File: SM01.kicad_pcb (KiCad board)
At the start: 2 copper layers, 150 parts, among them J1 TRIG IN, J2 TRIG IN, J3 TRIG IN, J4 DC JACK, J5 TRIG IN, J6 VCA IN, J7 MIXOUT, Q1 2N3904, SW1 HOLD, SW10 SPDT_small, SW11 SPDT_small, SW12 MOM, SW13 SPDT_small, SW14 MOM, SW15 MOM, SW16 MOM, SW17 MOM, SW18 MOM, SW19 MOM, SW2 HOLD, SW20 MOM, SW21 MASTERSW, SW3 HOLD, SW4 ON, SW5 MOM, SW6 MOM, SW7 MOM, SW8 HOLD, SW9 SPDT_small, U1 072, U10 072, U11 072, U2 072, U3 072, U4 7414, U5 7414, U6 7414, U8 072, U9 072

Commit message: organized channels
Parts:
- moved C27 260.7 mm to (100.3, 182.9)
- moved R39 249.5 mm to (113.0, 182.9)
- moved C23 242.9 mm to (100.3, 179.1)
- moved C20 235.9 mm to (100.3, 175.3)
- moved C15 209.2 mm to (108.0, 168.9)
- moved U6 206.0 mm to (101.6, 143.5)
- moved SW4 203.6 mm to (185.4, 143.5)
- moved LED3 201.2 mm to (114.3, 144.8)
- moved MASTERV1 200.7 mm to (222.2, 33.0)
- moved R17 196.5 mm to (106.7, 120.7)
- moved OSC3 196.2 mm to (105.4, 132.1)
- moved C12 194.1 mm to (100.3, 168.9)
- moved C30 193.0 mm to (115.6, 168.9)
- moved R23 191.2 mm to (120.7, 113.0)
- moved R7 190.4 mm to (200.7, 130.8)
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
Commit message: continued laying out pcb - having issue with zfoot.pretty
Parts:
- removed LED1, LED2, LED3: LED-C1-A2, 4ms-footprints:LED-C1-A2-3MM-VERT
- removed SW12, SW5, SW6, SW7: MOM, 4ms-footprints:SPDT-SUB
- added LEDSW1: DPDT-ILLUM, 4ms-footprints:BUTTON-LED-PB61303, F.Cu at (10.0, -10.0)
- added LEDSW2: DPDT-ILLUM, 4ms-footprints:BUTTON-LED-PB61303, F.Cu at (50.0, -10.0)
- added LEDSW3: DPDT-ILLUM, 4ms-footprints:BUTTON-LED-PB61303, F.Cu at (90.0, -10.0)
- added LEDSW4: DPDT-ILLUM, 4ms-footprints:BUTTON-LED-PB61303, F.Cu at (130.0, -10.0)
- added R50: 470, 4ms-footprints:Resistor_TH_300, B.Cu at (115.6, 63.7)
- C1, C10, C11, C12, C13, C14, C15, C16, C17, C18, C19, C2, C20, C21, C22, C23, C24, C25, C26, C27, C28, C29, C3, C30, C31, C32, C4, C5, C6, C7, C8, C9, D1, D2, D3, D4, D5, D6, J4, Q1, R1, R10, R11, R12, R13, R14, R15, R16, R17, R18, R19, R20, R21, R22, R23, R24, R25, R26, R27, R28, R29, R3, R30, R31, R32, R33, R34, R35, R36, R37, R38, R39, R4, R40, R41, R42, R43, R44, R45, R46, R47, R48, R49, R5, R6, R7, R8, R9, SW4, U1, U10, U11, U2, U3, U4, U5, U6, U8, U9, VREG1: moved to B.Cu
- SW10: value SPDT_small -> DECAYSW2
- SW11: value SPDT_small -> DECAYSW3
- SW13: value SPDT_small -> DECAYSW4
- SW14: value MOM -> OSCSW1
- SW15: value MOM -> OSCSW2
- SW16: value MOM -> OSCSW3
- SW17: value MOM -> MUTE4
- SW18: value MOM -> MUTE1
- SW19: value MOM -> MUTE2
- SW20: value MOM -> MUTE3
- SW9: value SPDT_small -> DECAYSW1
- moved VOL1 230.1 mm to (170.0, -85.0)
- moved C18 218.1 mm to (18.4, -28.9)
- moved R28 215.4 mm to (25.4, -40.6)
- moved C28 214.2 mm to (10.0, -46.8), turned to 90 degrees
- moved C10 213.5 mm to (30.0, -47.0), turned to 90 degrees
- moved C13 213.3 mm to (20.0, -46.9), turned to 90 degrees
- moved R21 207.9 mm to (30.0, -29.6), turned to 180 degrees
- moved J6 202.9 mm to (142.5, -95.0)
- moved SW20 199.7 mm to (190.0, -47.5)
- moved C25 193.9 mm to (21.6, -35.6)
- moved R15 193.2 mm to (12.5, -73.1), turned to 270 degrees
- moved C21 190.8 mm to (21.1, -7.39), turned to 90 degrees
- moved R31 189.5 mm to (18.5, -10.9), turned to 90 degrees
- moved R24 185.0 mm to (23.6, -10.9), turned to 90 degrees
- moved SW17 183.8 mm to (190.0, -28.8)
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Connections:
- R1 pad 1: Net-(R1-Pad1) -> Net-(J1-Pad1)
- R18 pad 1: Net-(R18-Pad1) -> Net-(J5-Pad1)
- R2 pad 1: Net-(R2-Pad1) -> Net-(J2-Pad1)
- R3 pad 1: Net-(R3-Pad1) -> Net-(J3-Pad1)
- SW1 pad 3: Net-(R1-Pad1) -> Net-(J1-Pad1)
- SW2 pad 3: Net-(R2-Pad1) -> Net-(J2-Pad1)
- SW3 pad 3: Net-(R3-Pad1) -> Net-(J3-Pad1)
- SW8 pad 3: Net-(R18-Pad1) -> Net-(J5-Pad1)
- U11 pad 5: Net-(U11-Pad5) -> Net-(ATTACK4-Pad2)
- U11 pad 6: Net-(U11-Pad6) -> LED_AR
- U11 pad 7: Net-(U11-Pad7) -> LED_AR
- U4 pad 14: Net-(U1-Pad6) -> Net-(C10-Pad1)
- U5 pad 14: Net-(U2-Pad6) -> Net-(C11-Pad1)
- U6 pad 14: Net-(U3-Pad6) -> Net-(C12-Pad1)
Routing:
- net GND: track 0.00 -> 65.7 mm, vias 0 -> 1
- net Net-(R1-Pad2): track 0.00 -> 16.5 mm, vias 0 -> 2
- net Net-(J1-Pad1): track 0.00 -> 9.36 mm
- net Net-(ATTACK1-Pad2): track 0.00 -> 7.31 mm
- net Net-(D2-Pad2): track 0.00 -> 5.84 mm
- net Net-(ATTACK1-Pad1): track 0.00 -> 4.01 mm
- net Net-(U1-Pad6): track 0.00 -> 2.54 mm
- net Net-(DECAY1-Pad1): track 0.00 -> 2.29 mm
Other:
- board outline added: 200 x 100 mm
- net class Default: clearance 0.2 -> 0
- rule trace_clearance: 0.2 -> 0

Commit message: finished placing components - starting to connect traces
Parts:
- added J10: EXP3, zfoot:Jack_Instrument_exp, F.Cu at (102.6, -95.0)
- added J8: EXP1, zfoot:Jack_Instrument_exp, F.Cu at (22.6, -95.0)
- added J9: EXP2, zfoot:Jack_Instrument_exp, F.Cu at (62.7, -95.0)
- J4, SW4: moved to F.Cu
- R2: moved to B.Cu
- moved R38 266.3 mm to (181.0, -54.1)
- moved C32 211.5 mm to (158.8, -51.1)
- moved C11 210.2 mm to (70.0, -47.0), turned to 90 degrees
- moved C12 209.9 mm to (110.0, -47.0), turned to 90 degrees
- moved C14 208.5 mm to (60.0, -47.0), turned to 90 degrees
- moved C29 208.4 mm to (50.0, -47.0), turned to 90 degrees
- moved C15 208.4 mm to (100.0, -47.0), turned to 90 degrees
- moved C30 208.3 mm to (90.0, -47.0), turned to 90 degrees
- moved R39 205.6 mm to (191.0, -34.8), turned to 180 degrees
- moved U8 202.1 mm to (145.0, -69.0), turned to 90 degrees
- moved R3 201.6 mm to (100.0, -85.0), turned to 270 degrees
- moved U3 201.3 mm to (105.0, -69.0), turned to 90 degrees
- moved U2 201.3 mm to (65.0, -69.0), turned to 90 degrees
- moved R18 200.7 mm to (140.0, -85.0), turned to 270 degrees
- moved R48 193.9 mm to (151.4, -51.1), turned to 180 degrees
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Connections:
- VOL1 pad 1: Net-(R40-Pad1) -> Net-(R41-Pad1)
- VOL1 pad 2: Net-(R44-Pad2) -> Net-(R45-Pad2)
- VOL2 pad 1: Net-(R41-Pad1) -> Net-(R42-Pad1)
- VOL2 pad 2: Net-(R45-Pad2) -> Net-(R46-Pad2)
- VOL3 pad 1: Net-(R42-Pad1) -> Net-(R43-Pad1)
- VOL3 pad 2: Net-(R46-Pad2) -> Net-(R47-Pad2)
- VOL4 pad 1: Net-(R43-Pad1) -> Net-(R40-Pad1)
- VOL4 pad 2: Net-(R47-Pad2) -> Net-(R44-Pad2)
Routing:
- net GND: track 65.7 -> 0.85 mm, vias 1 -> 0
- net Net-(R1-Pad2): track 16.5 -> 0.00 mm, vias 2 -> 0
- net Net-(J1-Pad1): track 9.36 -> 0.01 mm
- net Net-(ATTACK1-Pad2): track 7.31 -> 2.65 mm
- net Net-(ATTACK1-Pad1): track 4.01 -> 0.40 mm
- net Net-(D2-Pad2): track 5.84 -> 3.15 mm
- net Net-(J8-Pad1): track 0.00 -> 2.54 mm
- net Net-(U1-Pad6): track 2.54 -> 0.00 mm
- net Net-(DECAY1-Pad1): track 2.29 -> 0.03 mm

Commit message: finished channel 1 but theres so much more bullshit left
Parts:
- moved J4 19.6 mm to (195.3, -95.0)
- moved SW4 5.00 mm to (180.0, -95.0)
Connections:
- J10 pad 2: Net-(J10-Pad1) -> Net-(J10-Pad2)
- J8 pad 2: Net-(J8-Pad1) -> Net-(J8-Pad2)
- J9 pad 2: Net-(J9-Pad1) -> Net-(J9-Pad2)
- R37 pad 1: Net-(J8-Pad1) -> Net-(J8-Pad2)
- R38 pad 1: Net-(J9-Pad1) -> Net-(J9-Pad2)
- R39 pad 1: Net-(J10-Pad1) -> Net-(J10-Pad2)
- U4 pad 6: Net-(J8-Pad1) -> Net-(J8-Pad2)
- U5 pad 6: Net-(J9-Pad1) -> Net-(J9-Pad2)
- U6 pad 6: Net-(J10-Pad1) -> Net-(J10-Pad2)
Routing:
- net GND: track 0.85 -> 913.8 mm, vias 0 -> 46
- net +5V: track 0.00 -> 687.0 mm, vias 0 -> 25
- net Net-(J8-Pad2): track 0.00 -> 295.2 mm, vias 0 -> 9
- net Net-(J1-Pad1): track 0.01 -> 131.5 mm, vias 0 -> 5
- net Net-(D1-Pad2): track 0.00 -> 108.2 mm, vias 0 -> 6
- net Net-(R48-Pad2): track 0.00 -> 95.8 mm, vias 0 -> 4
- net Net-(J8-Pad1): track 2.54 -> 75.3 mm, vias 0 -> 3
- net Net-(C25-Pad1): track 0.00 -> 67.5 mm, vias 0 -> 5
- net Net-(C13-Pad1): track 0.00 -> 55.5 mm, vias 0 -> 3
- net Net-(ATTACK1-Pad2): track 2.65 -> 54.9 mm, vias 0 -> 3
- net 2.5v: track 0.00 -> 50.0 mm, vias 0 -> 4
- net Net-(J5-Pad1): track 0.00 -> 42.7 mm, vias 0 -> 5
- net Net-(R1-Pad2): track 0.00 -> 42.7 mm, vias 0 -> 3
- net Net-(R41-Pad1): track 0.00 -> 38.9 mm, vias 0 -> 3
- net Net-(R45-Pad2): track 0.00 -> 37.7 mm, vias 0 -> 1
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
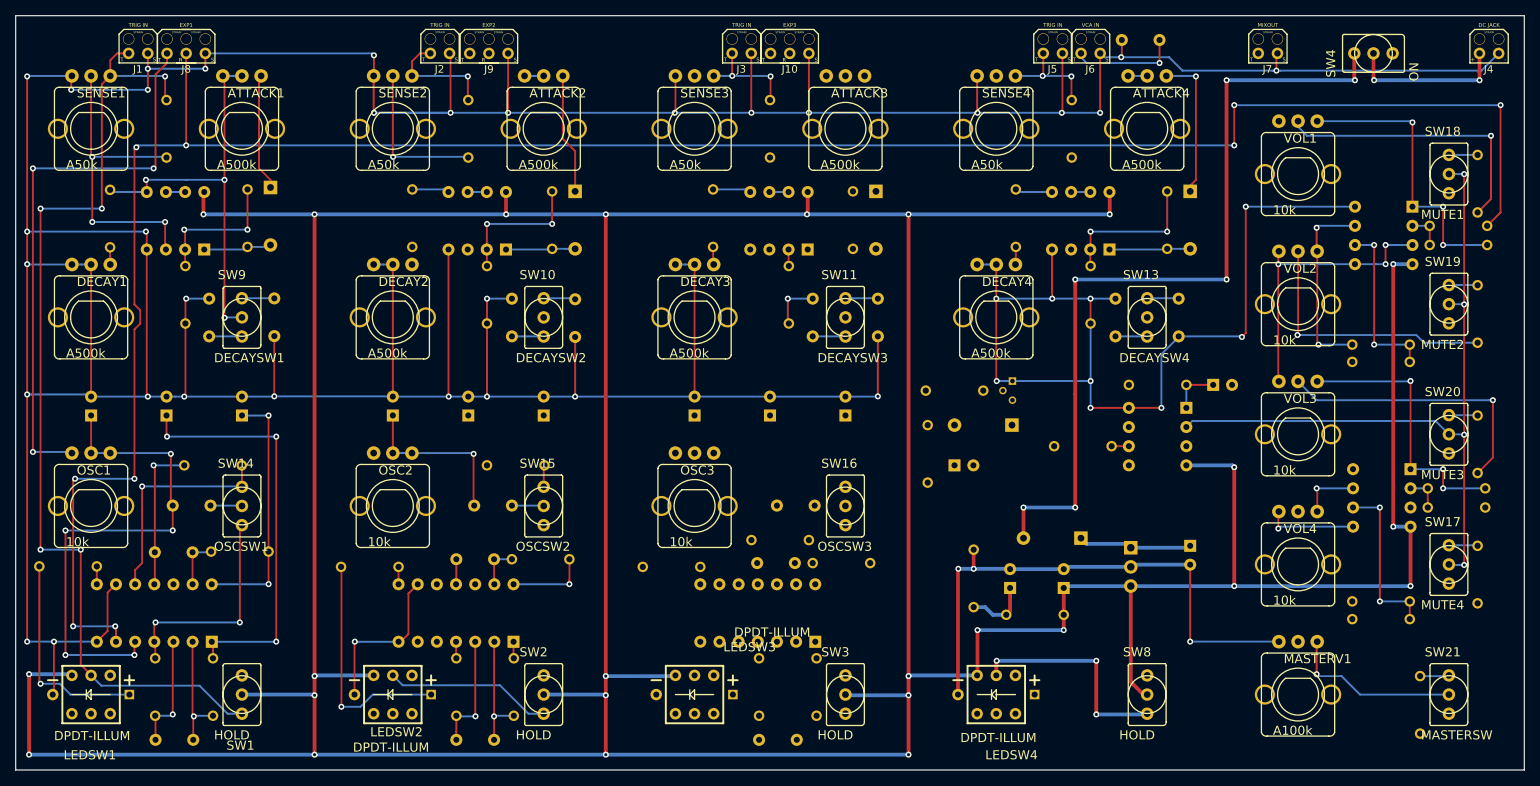
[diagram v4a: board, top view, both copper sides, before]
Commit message: finished laying traces and organizing ref
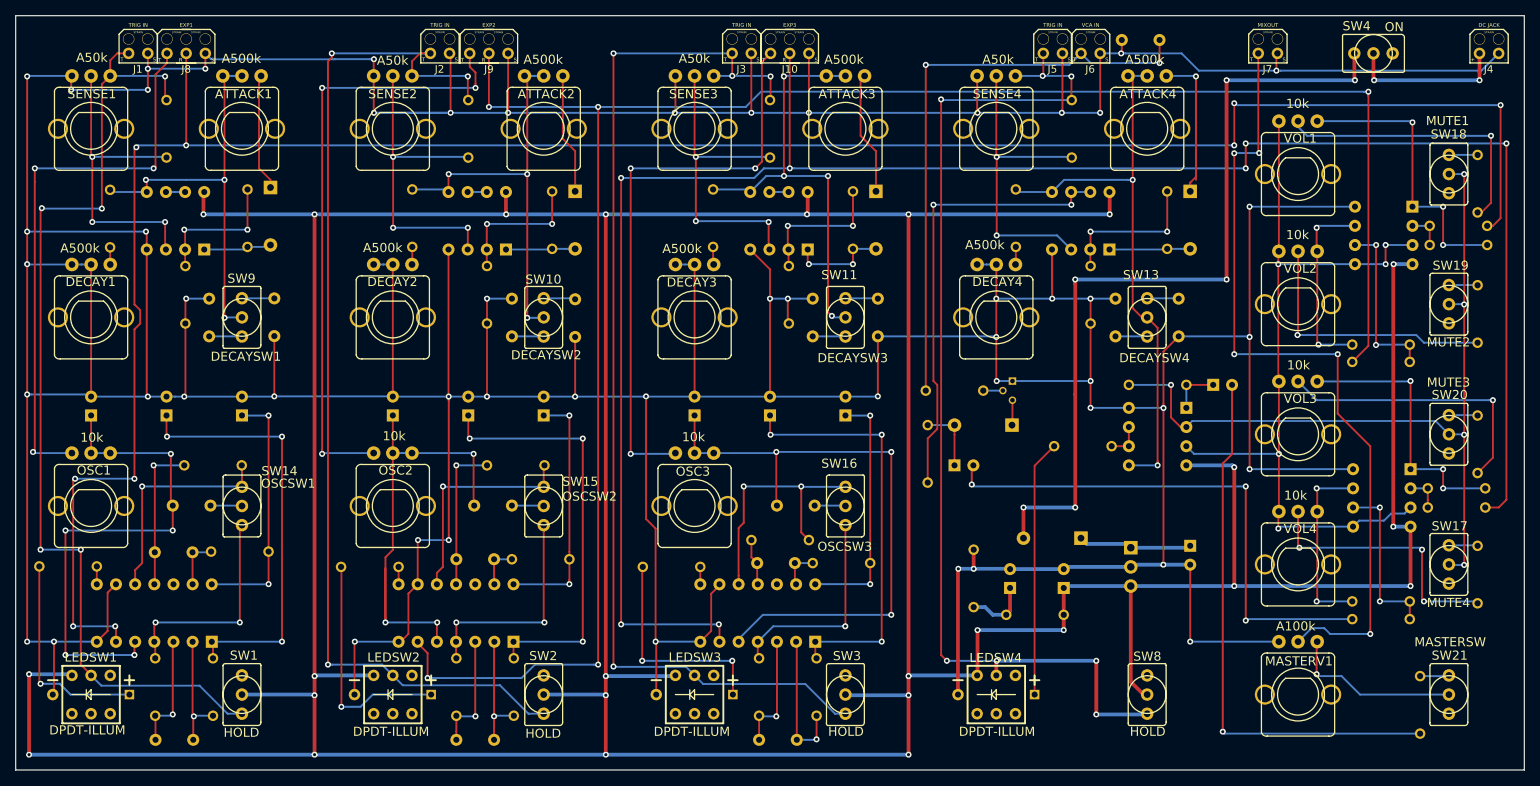
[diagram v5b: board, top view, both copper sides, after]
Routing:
- net Net-(J9-Pad2): track 0.00 -> 263.8 mm, vias 0 -> 5
- net Net-(J10-Pad2): track 0.00 -> 261.4 mm, vias 0 -> 7
- net GND: track 913.8 -> 1088.2 mm, vias 46 -> 54
- net Net-(J3-Pad1): track 13.7 -> 144.1 mm, vias 2 -> 4
- net Net-(J7-Pad1): track 0.00 -> 106.4 mm, vias 0 -> 5
- net Net-(J2-Pad1): track 37.5 -> 141.0 mm, vias 1 -> 3
- net Net-(J5-Pad1): track 42.7 -> 141.4 mm, vias 5 -> 7
- net Net-(C27-Pad1): track 0.00 -> 81.8 mm, vias 0 -> 3
- net Net-(J9-Pad1): track 0.00 -> 80.6 mm, vias 0 -> 3
- net Net-(J10-Pad1): track 0.00 -> 76.4 mm, vias 0 -> 3
- net Net-(C32-Pad2): track 0.00 -> 72.8 mm, vias 0 -> 1
- net Net-(C31-Pad2): track 0.00 -> 71.0 mm, vias 0 -> 3
- net Net-(ATTACK4-Pad2): track 7.47 -> 76.3 mm, vias 0 -> 2
- net Net-(C24-Pad1): track 14.3 -> 78.4 mm, vias 1 -> 2
- net Net-(R35-Pad2): track 2.54 -> 60.1 mm, vias 0 -> 2
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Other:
- net class Default: clearance 0 -> 0.25
- rule trace_clearance: 0 -> 0.25
- board text added: "DRT SM01 v1.0"

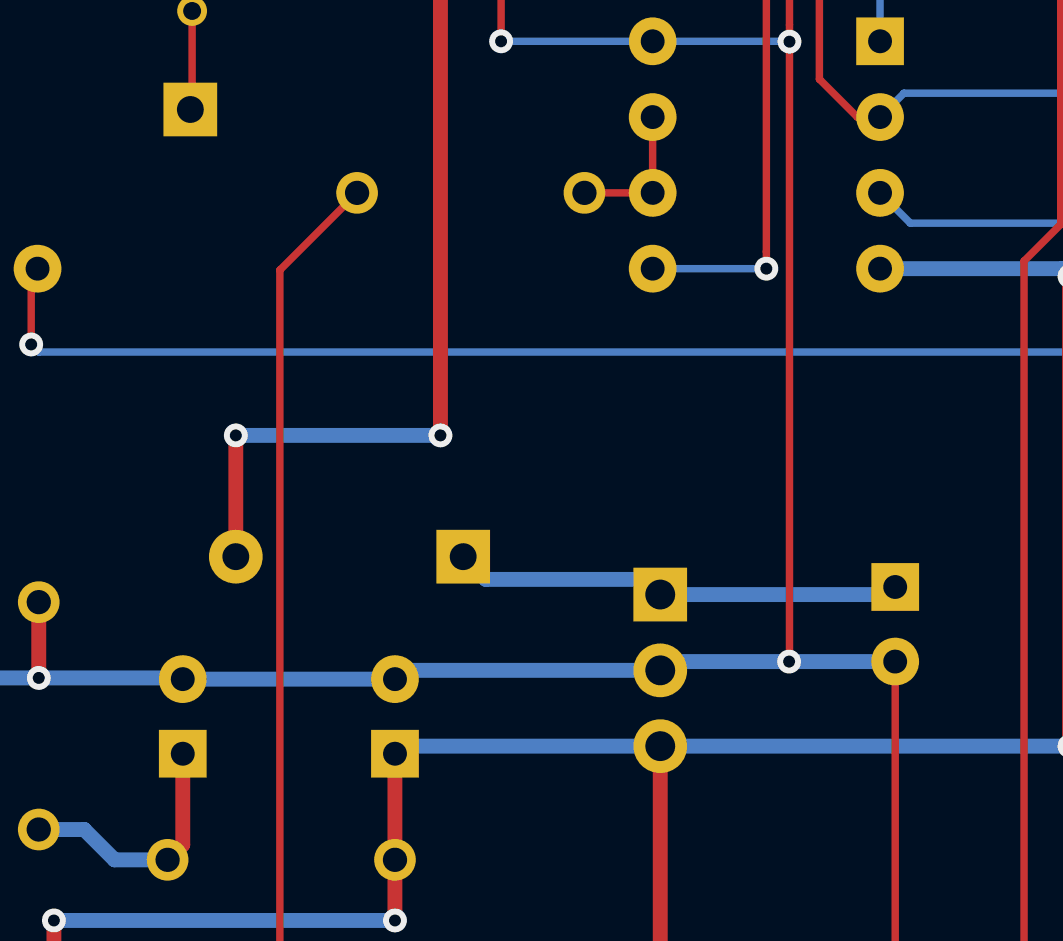
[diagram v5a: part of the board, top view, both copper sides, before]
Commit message: fixed 2.5v tag issue
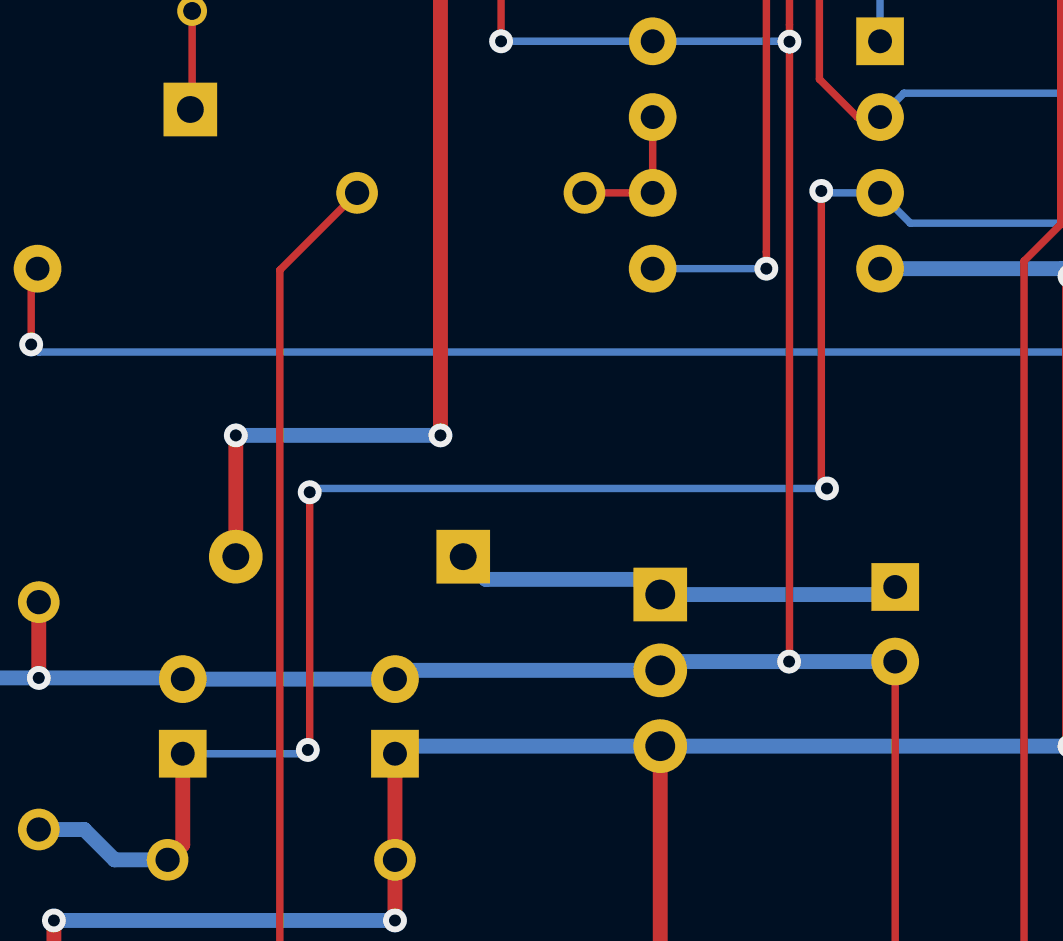
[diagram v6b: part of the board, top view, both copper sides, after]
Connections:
- C3 pad 1: 2.5V -> 2.5v
- R7 pad 2: 2.5V -> 2.5v
- R8 pad 1: 2.5V -> 2.5v
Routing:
- net 2.5v: track 105.9 -> 156.7 mm, vias 5 -> 9
- net 2.5V: track 8.51 -> 0.00 mm

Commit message: added gbr - sent file in -HOPE IT WORKS!
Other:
- board text added: "can use jumper maybe?"
- board text added: "optional"
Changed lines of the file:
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@@
   (general
     (thickness 1.6)
-    (drawings 5)
+    (drawings 8)
     (tracks 1336)
     (zones 0)
@@
     (35 F.Paste user)
     (36 B.SilkS user)
-    (37 F.SilkS user hide)
+    (37 F.SilkS user)
     (38 B.Mask user)
     (39 F.Mask user)
@@
     (visible_elements 7FFFEFFF)
     (pcbplotparams
-      (layerselection 0x00030_ffffffff)
+      (layerselection 0x010f8_ffffffff)
       (usegerberextensions false)
       (usegerberattributes true)
@@
       (viasonmask false)
       (mode 1)
-      (useauxorigin false)
+      (useauxorigin true)
       (hpglpennumber 1)
       (hpglpenspeed 20)
@@
       (outputformat 1)
       (mirror false)
-      (drillshape 1)
+      (drillshape 0)
       (scaleselection 1)
-      (outputdirectory ""))
+      (outputdirectory gbr/))
   )
   (net 0 "")
@@
     (pad "" thru_hole circle (at 1.27 -1.905) (size 1.524 1.524) (drill 1.4) (layers *.Cu *.Mask))
   )
+  (target plus (at 0 0) (size 5) (width 0.15) (layer Edge.Cuts))
+  (gr_text "can use jumper maybe?" (at 182.499 -17.3355) (layer B.SilkS)
+    (effects (font (size 0.75 0.75) (thickness 0.1875)) (justify mirror))
+  )
+  (gr_text optional (at 154.7495 -96.8375) (layer B.SilkS)
+    (effects (font (size 0.5 0.5) (thickness 0.125)) (justify mirror))
+  )
   (gr_text "DRT SM01 v1.0" (at 151.3205 -3.302) (layer B.SilkS)
